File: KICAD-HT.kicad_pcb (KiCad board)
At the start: 2 copper layers, 128.8 x 60 mm, 126 parts, among them J1 HV80_IN, J2 NAPPE_FILAMENT_HT, Q1 IPD050N10N5, Q2 IPD050N10N5, Q3 BSS127I, Q4 MMBT2222, Q5 BSS127I, T1 MSD1514-103ME, U1 UCC27517, U10 ISO7710, U11 AMC0311R, U12 UCC24612, U13 SN74LVC1G08, U14 TSV791, U15 ATL431, U16 LMV7219, U17 SN74LVC1G132, U18 SN74LVC1G74, U19 ISO7710F, U3 ISO7710, U5 DPC817, U7 AMC0311R, U8 AMC0311R, U9 AMC0302R

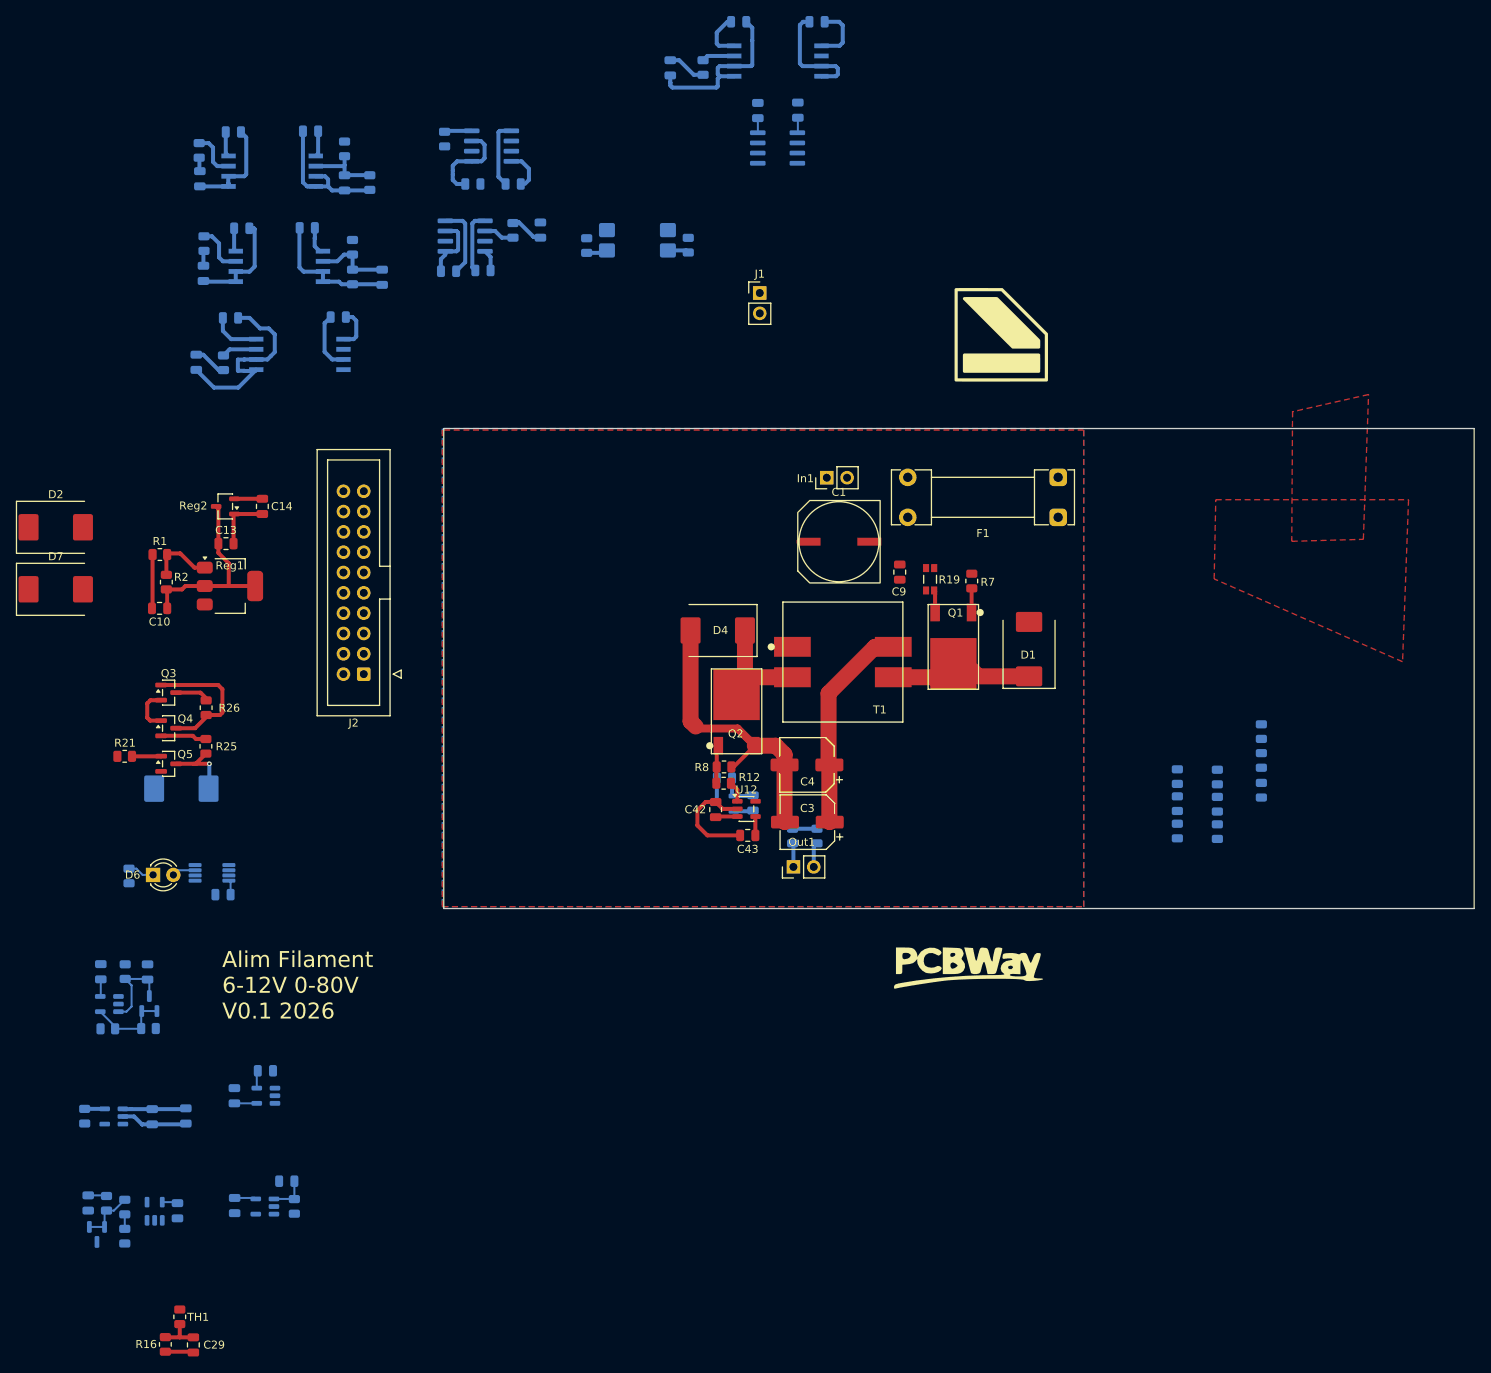
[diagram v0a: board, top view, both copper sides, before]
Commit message: Retire la barriere d'isolation primaire/secondaire (secondaire non isole du primaire dans le montage final)
Decision utilisateur du 2026-10-25 : le secondaire de puissance (VOUT_N/
VOUT_P) ne sera plus flottant ni isole galvaniquement du primaire. La
regle .kicad_dru barriere_primaire_secondaire est retiree (commentee,
pas supprimee), la classe de nets SEC est conservee a titre
organisationnel dans KICAD-HT.kicad_pro. Seule la barriere controle
(C2000) <-> puissance reste une isolation reelle. 00-intention-conception.md,
README.md et doc/plan-isolation-4couches.md mis a jour (section 20bis).
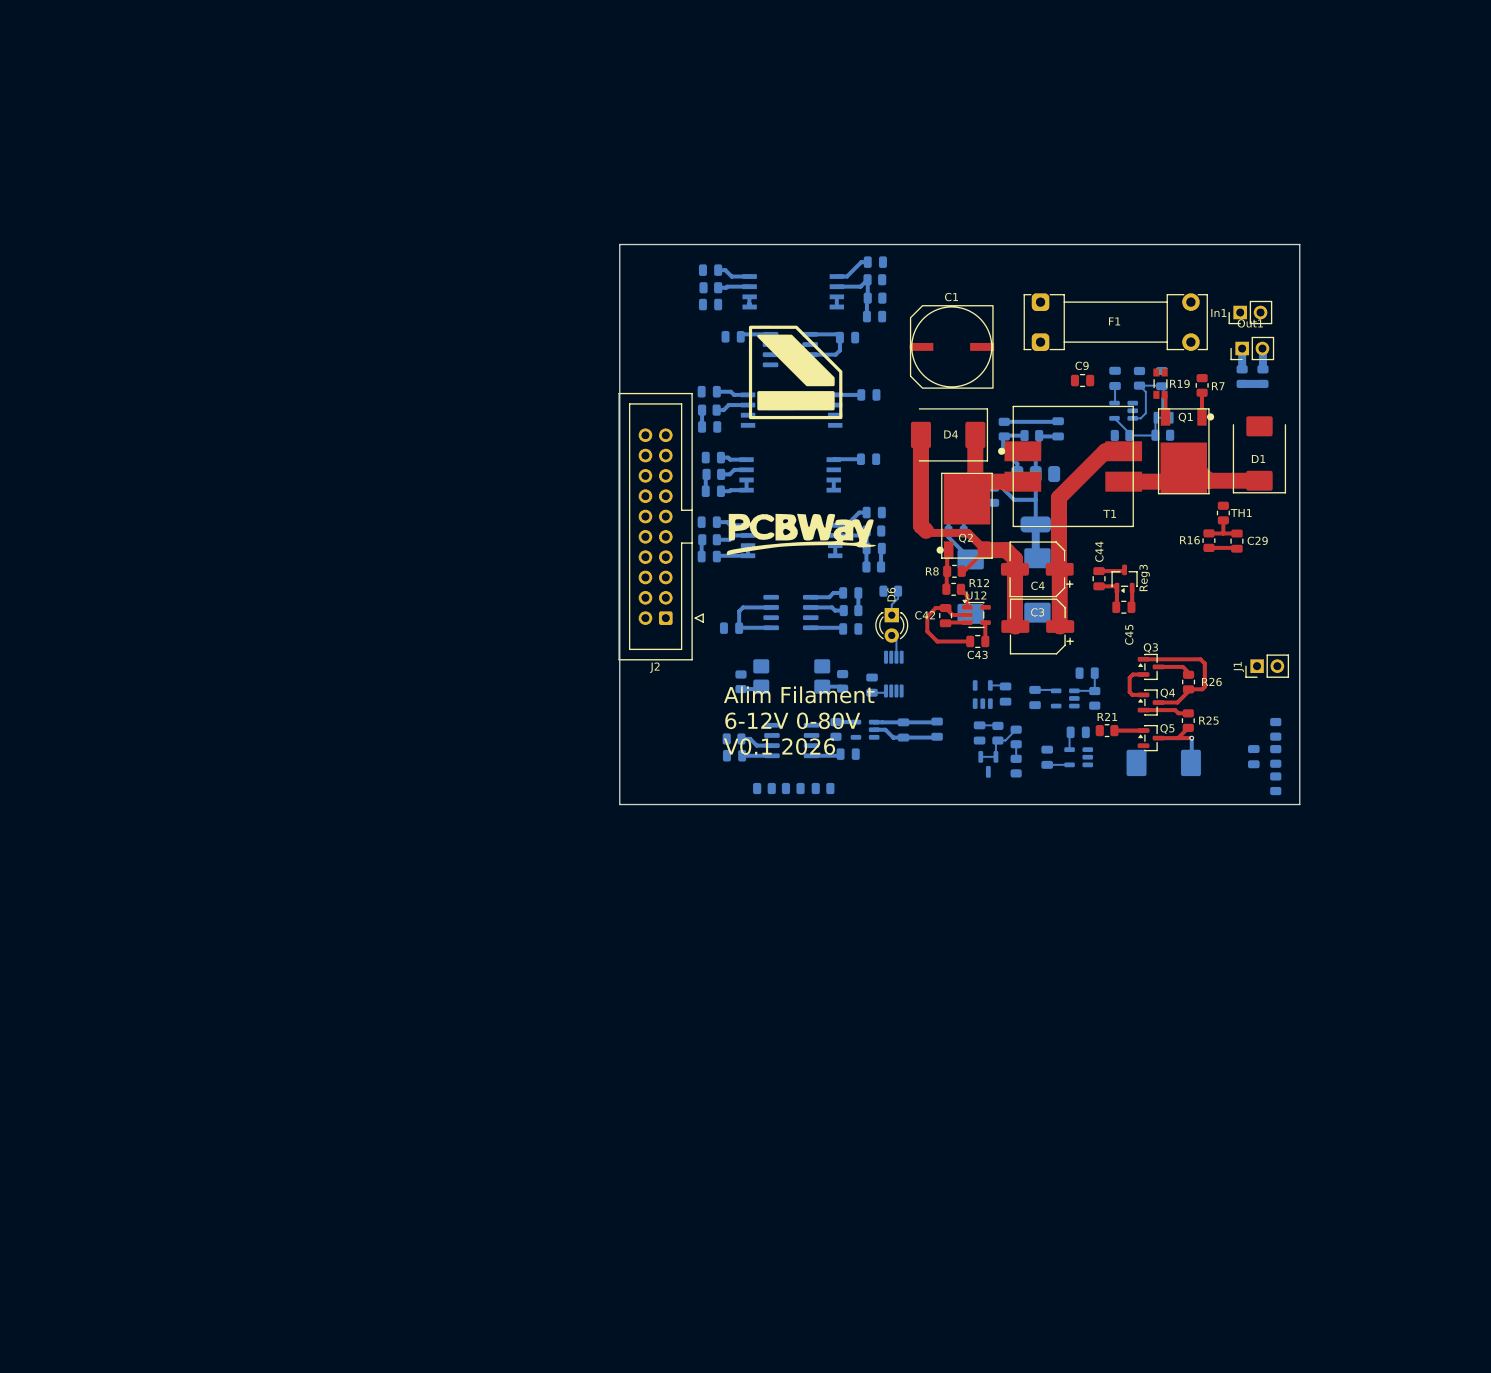
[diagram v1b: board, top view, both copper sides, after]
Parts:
- removed R35, R36, R6: 1M, Resistor_SMD:R_0805_2012Metric
- added C27: 100n, Capacitor_SMD:C_0805_2012Metric, B.Cu at (174.3, 111.0)
- C10, C13, C14, D2, D7, R1, R2, Reg1, Reg2: moved to B.Cu
- C44, C45, Reg3: moved to F.Cu
- F1: value Fuse -> 3A
- moved C29 164.7 mm to (172.2, 84.1)
- moved R16 164.7 mm to (168.7, 84.0)
- moved TH1 164.7 mm to (170.4, 80.6)
- moved U14 146.9 mm to (158.0, 67.8)
- moved C47 146.9 mm to (162.8, 63.8)
- moved C48 146.9 mm to (156.9, 63.7)
- moved R27 146.9 mm to (160.0, 63.7)
- moved D5 146.9 mm to (163.0, 67.7)
- moved R28 146.9 mm to (157.8, 70.9)
- moved R29 146.9 mm to (162.9, 70.8)
- moved C55 126.0 mm to (140.0, 108.0)
- moved R30 126.0 mm to (142.3, 108.1)
- moved R31 126.0 mm to (144.6, 108.6)
- moved R32 126.0 mm to (144.6, 112.2)
- moved U15 126.0 mm to (141.1, 112.0)
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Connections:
- R40 pad 2: VOUT_N -> HV_BIAS
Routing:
- net GND_CTRL: track 86.1 -> 11.0 mm
- net GND: track 81.5 -> 32.8 mm
- net VOUT_N: track 75.4 -> 61.9 mm
- net RAIL_3V3_PRI: track 41.8 -> 49.8 mm
- net 3V3_ISO: track 39.9 -> 33.6 mm
- net RAIL_8V25: track 32.6 -> 37.0 mm
- net PWM_ht: track 0.00 -> 4.17 mm
- net I_Shunt_ht: track 4.86 -> 2.10 mm
- net VAR_GATE: track 8.30 -> 5.85 mm
- net VOUT_FBACK_RAW: track 6.29 -> 4.12 mm
- net Temp_ht: track 4.20 -> 2.14 mm
- net Net-(U11-OUT): track 5.91 -> 3.99 mm
- net V_bias: track 1.54 -> 0.00 mm
- net Net-(U8-OUT): track 4.42 -> 3.41 mm
- net RAIL_3V3_SEC: track 6.02 -> 7.01 mm
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- removed copper zone on B.Cu, net GND
- removed copper zone on F.Cu, net GND
- removed copper zone on F.Cu, net GND_CTRL
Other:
- board size 128.8 x 60 mm -> 85 x 70 mm
